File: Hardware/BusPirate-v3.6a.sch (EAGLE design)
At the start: 43 parts, among them IC1 PIC24FJ64GA002, IC2 FT232RL-BASICSSOP, IC3 4066

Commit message: Finished inital DFM
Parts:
- removed IC3: 4066, 40xx:4066
- removed ICSP: (no value), SparkFun-Connectors:M05PTH
- removed LED1A, LED2A, LED3A, LED4A: (no value), led:LEDCHIP-LED0805
- removed RN1, RN2: 10k, Testing:CAY16-F4
- removed VR3: MIC5205 5V0, SparkFun-PowerIC:MIC52055V
- added JP2: (no value), SparkFun-Connectors:M05PTH
- added LED5, LED6, LED7, LED8: RED, SparkFun-LED:LED-RED0603
- added R10, R11: 2.0k, SparkFun-Resistors:2.0KOHM1/10W5%(0603)
- added R7, R9: 1K, SparkFun-Resistors:1KOHM-1/10W-1%(0603)
- added R8: 0.27, SparkFun-Resistors:0OHM-1/10W-5%(0603)
- added U3: PIC24FJ64GA002, Testing:PIC24FJ64GA002
- added U4: MIC5205 5V0, SparkFun-PowerIC:MIC52055V
- C10, C11: value 10uF -> 0.1uF; device rcl:CPOL-EUSMCA -> SparkFun-Capacitors:0.1UF-25V(+80/-20%)(0603)
- C3, C4, C7: value 0.1uF -> 10uF; device SparkFun-Capacitors:0.1UF-25V(+80/-20%)(0603) -> SparkFun-Capacitors:10UF10V10%(0805)
- C5: device dp_devices:CAPC603 -> SparkFun-Capacitors:0.1UF-25V(+80/-20%)(0603)
- C8, C9: value 1uF -> 10uF; device dp_devices:CAPC603 -> SparkFun-Capacitors:10UF10V10%(0805)
- IC1: value PIC24FJ64GA002 -> 4066; device dp_devices:PIC24FJ64GA002 -> 40xx:4066; PROD_ID (none) -> IC-09427
- JP1: PROD_ID (none) -> CONN-09508
- L1: value 700mA+ ferrite -> 1A Ferrite; device wuerth-elektronik:WE-KIL_0805 -> SparkFun-Passives:INDUCTOR0603; PROD_ID (none) -> NDUC-12579
- LED1: value (none) -> RED; device led:LEDCHIP-LED0805 -> SparkFun-LED:LED-RED0603; PROD_ID (none) -> DIO-00819
- LED2, LED3, LED4: value (none) -> RED; device led:LEDCHIP-LED0805 -> SparkFun-LED:LED-RED0603
- LOGO1: value SFE_LOGO_NAME_FLAME.1_INCH -> OSHW-LOGOL; device SparkFun-Aesthetics:SFE_LOGO_NAME_FLAME.1_INCH -> SparkFun-Aesthetics:OSHW-LOGOL
- LOGO2: value OSHW-LOGOL -> SFE_LOGO_NAME_FLAME.1_INCH; device SparkFun-Aesthetics:OSHW-LOGOL -> SparkFun-Aesthetics:SFE_LOGO_NAME_FLAME.1_INCH
- R1, R5: value 2.0k -> 0.27; device SparkFun-Resistors:2.0KOHM1/10W5%(0603) -> SparkFun-Resistors:0OHM-1/10W-5%(0603); PROD_ID (none) -> RES-08787
- R2, R3: value 1K -> 10k; device SparkFun-Resistors:1KOHM-1/10W-1%(0603) -> Testing:CAY16-F4; PROD_ID (none) -> RES-13167
- U5: PROD_ID (none) -> IC-00870
- renumbered IC2 to U5, RN3 to R12, U$2 to J1, VR1 to U1, VR2 to U2
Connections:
- new net N$10: C7.2, R5.2
- new net N$11: C8.2, R8.2
- new net N$8: C3.2, R1.2
- net !MCLR: now also JP2.5, R10.1, U3.MCLR; no longer IC1.MCLR, ICSP.5, R1.1
- net 5V: now also C5.1, C6.1, IC1P.VDD, U4.IN; no longer C10.+, C3.1, IC3P.VDD, VR3.IN
- net ADC: now also R3C.2; no longer RN2C.2
- net ADC1: now also R3C.1, R3D.1, U3.PMD0/CN14/RP12/AN12/RB12; no longer IC1.PMD0/CN14/RP12/AN12/RB12, RN2C.1, RN2D.1
- net ADC2: now also R3A.1, R3B.1, U3.PMRD/CN13/RP13/AN11/RB13; no longer IC1.PMRD/CN13/RP13/AN11/RB13, RN2A.1, RN2B.1
- net ADC3: now also R2C.1, R2D.1, U3.PMWR/RTCC/CVREF/CN12/RP14/AN10/RB14; no longer IC1.PMWR/RTCC/CVREF/CN12/RP14/AN10/RB14, RN1C.1, RN1D.1
- net ADC4: now also R2A.1, R2B.1, U3.PMCS1/CN11/RP15/AN9/RB15; no longer IC1.PMCS1/CN11/RP15/AN9/RB15, RN1A.1, RN1B.1
- net AUX1: now also U3.PMD2/TDI/EMUD2/PGD2/CN16/RP10/RB10; no longer IC1.PMD2/TDI/EMUD2/PGD2/CN16/RP10/RB10
- net CLK: now also U3.PMD4/SCL1/TCK/CN22/RP8/RB8; no longer IC1.PMD4/SCL1/TCK/CN22/RP8/RB8
- net CS: now also U3.PMD6/ASCL1/EMUC3/PGC3/CN24/RP6/RB6; no longer IC1.PMD6/ASCL1/EMUC3/PGC3/CN24/RP6/RB6
- net CTS: now also U3.RA3/CN29/OSCO/CLKO/PMA0; no longer IC1.RA3/CN29/OSCO/CLKO/PMA0
- net GND: now also C10.2, C11.2, IC1P.VSS, JP2.3, LED4.C, LED5.C, LED6.C, LED7.C, LED8.C, R1.1, R2B.2, R2D.2, R3B.2, R3D.2, R5.1, R8.1, U3.DISVREG, U3.RB2/AN4/RP2/CN6/C1IN-/SDA2, U3.RB3/AN5/RP3/CN7/C1IN+/SCL2, U3.VSS@1, U3.VSS@2, U4.GND; no longer C10.-, C11.-, C3.2, C7.2, C8.2, IC1.DISVREG, IC1.RB2/AN4/RP2/CN6/C1IN-/SDA2, IC1.RB3/AN5/RP3/CN7/C1IN+/SCL2, IC1.VSS@1, IC1.VSS@2, IC3P.VSS, ICSP.3, LED1.C, LED1A.C, LED2.C, LED2A.C, LED3A.C, RN1B.2, RN1D.2, RN2B.2, RN2D.2, VR3.GND
- net LD1: now also R7.2, U3.RA1/AN1/CN3/VREF-; no longer IC1.RA1/AN1/CN3/VREF-, R4.2
- net MISO: now also U3.PMD5/INT0/CN23/RP7/RB7; no longer IC1.PMD5/INT0/CN23/RP7/RB7
- net MOSI: now also R11.1, U3.PMD3/SDA1/TDO/CN21/RP9/RB9; no longer IC1.PMD3/SDA1/TDO/CN21/RP9/RB9, R5.1
- net N$1: now also IC1A.B, R11.2; no longer IC3A.B, R5.2
- net N$13: now also LED1.A, LED2.A, R4.1; no longer LED4.A, LED4A.A, R3.1
- net N$18: now also LED7.A, LED8.A, R9.1; no longer LED3.A, LED3A.A, R6.1
- net N$2: now also IC1C.B; no longer IC3C.B
- net N$3: now also C9.1, U3.VCAP/VDDCORE; no longer C11.+, IC1.VCAP/VDDCORE
- net N$4: now also IC1D.B; no longer IC3D.B
- net N$5: now also IC1B.B; no longer IC3B.B
- net N$6: now also LED5.A, LED6.A, R7.1; no longer LED2.A, LED2A.A, R4.1
- net N$7: now also LED3.A, LED4.A, R6.1; no longer LED1.A, LED1A.A, R2.1
- net N$9: now also C11.1; no longer C5.1
- net PGC: now also JP2.1, U3.RB1/AN3/RP1/CN5/C2IN+/PGC1/EMUC1; no longer IC1.RB1/AN3/RP1/CN5/C2IN+/PGC1/EMUC1, ICSP.1
- net PGD: now also JP2.2, U3.RB0/AN2/RP0/CN4/C2IN-/PGD1/EMUD1; no longer IC1.RB0/AN2/RP0/CN4/C2IN-/PGD1/EMUD1, ICSP.2
- net PULLUPEN: now also IC1A.C, IC1B.C, IC1C.C, IC1D.C, U3.PMD1/TMS/EMUC2/PGC2/CN15/RP11/RB11; no longer IC1.PMD1/TMS/EMUC2/PGC2/CN15/RP11/RB11, IC3A.C, IC3B.C, IC3C.C, IC3D.C
- net RTS: now also U3.RA4/CN0/SOSCO/T1CK/PMA1; no longer IC1.RA4/CN0/SOSCO/T1CK/PMA1
- net RX: now also U3.RB4/RP4/CN1/SOSCI/PMBE; no longer IC1.RB4/RP4/CN1/SOSCI/PMBE
- net RXLED: now also LED1.C, LED2.C; no longer LED4.C, LED4A.C
- net SW3V3: now also C7.1, R2C.2, R9.2; no longer C8.1, R6.2, RN1C.2
- net SW5V0: now also C8.1, R2A.2, U4.OUT; no longer C9.1, RN1A.2, VR3.OUT
- net TP0: now also U3.RA2/CN30/OSCI/CLKI; no longer IC1.RA2/CN30/OSCI/CLKI
- net TX: now also U3.RB5/RP5/CN27/PGD3/EMUD3/ASDA1/PMD7; no longer IC1.RB5/RP5/CN27/PGD3/EMUD3/ASDA1/PMD7
- net VCC: now also C10.1, C3.1, JP2.4, R10.2, R4.2, R6.2, U3.VDD@1, U3.VDD@2; no longer C6.1, C7.1, IC1.VDD@1, IC1.VDD@2, ICSP.4, R1.2, R2.2, R3.2
- net VEXTERN: now also IC1A.A, IC1B.A, IC1C.A, IC1D.A, R3A.2; no longer IC3A.A, IC3B.A, IC3C.A, IC3D.A, RN2A.2
- net VREGEN: now also U3.RA0/AN0/CN2/VREF+, U4.EN; no longer IC1.RA0/AN0/CN2/VREF+, VR3.EN
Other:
- note added: "CABLE CONNECTOR"
- note added: "The MIC5205 requires some ESR, added 0.27Ω"
- moved on the sheet: C1, C2, C3, C4, C5, C6, C7, C8, C9, JP1, R1, R4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

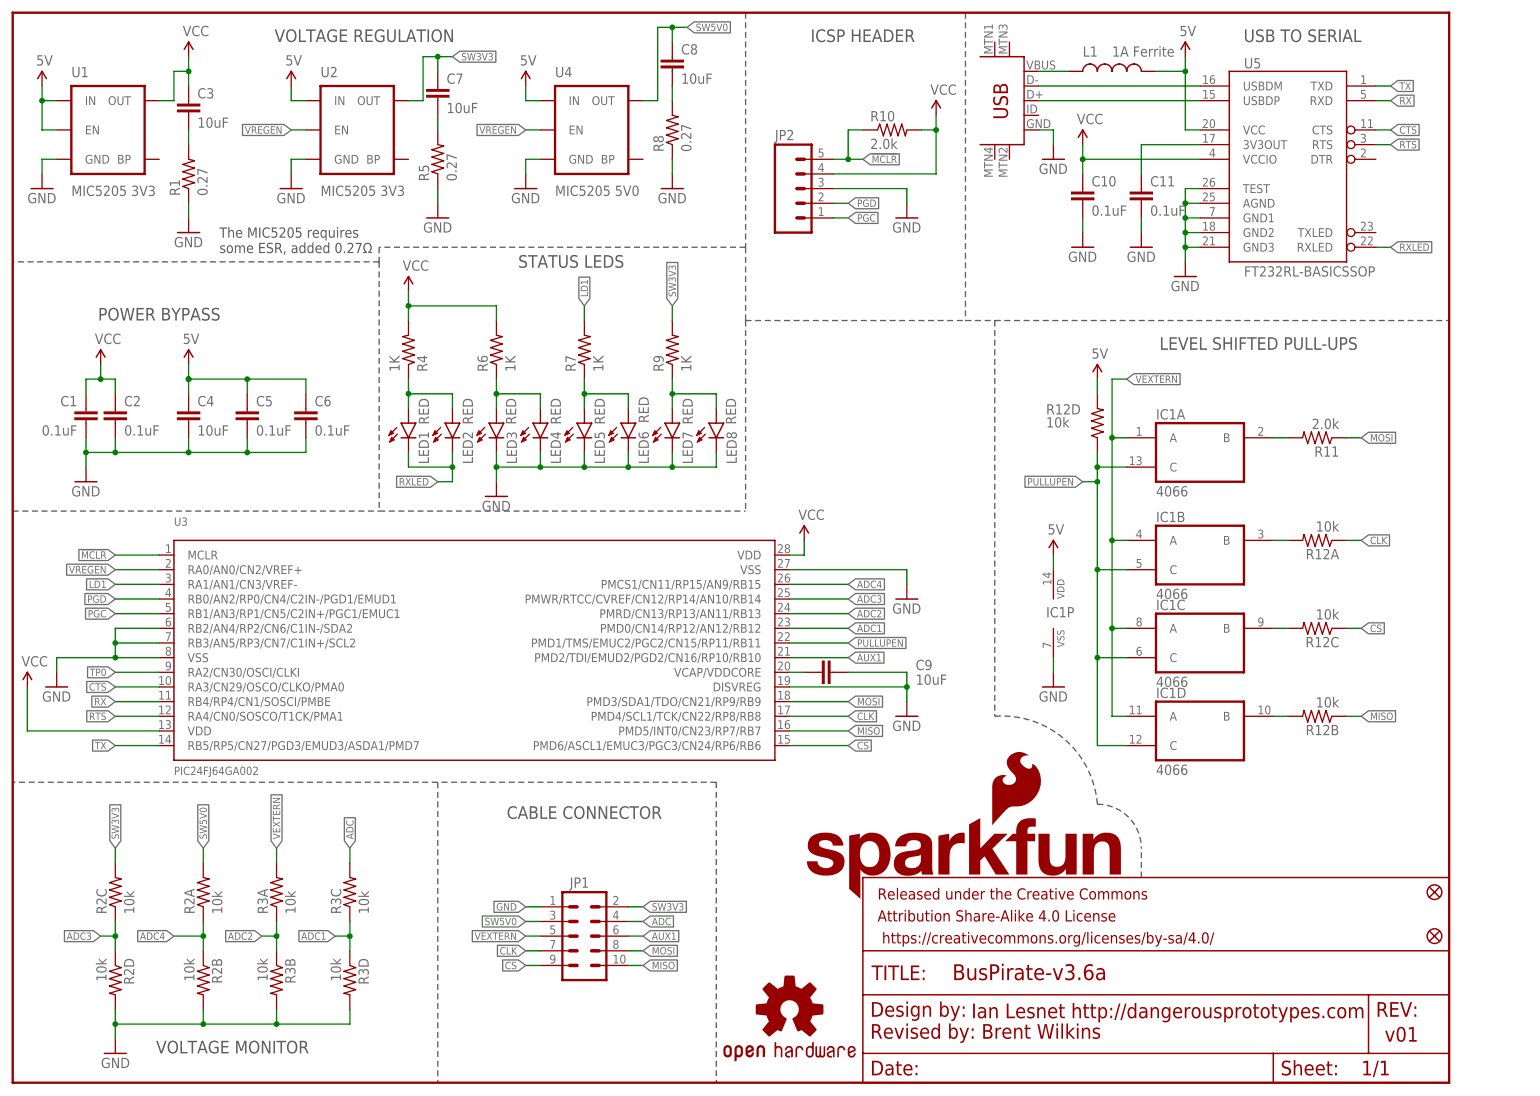
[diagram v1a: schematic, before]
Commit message: Changed from SFE to DP versioning, and changed bottom LEDs to DNP
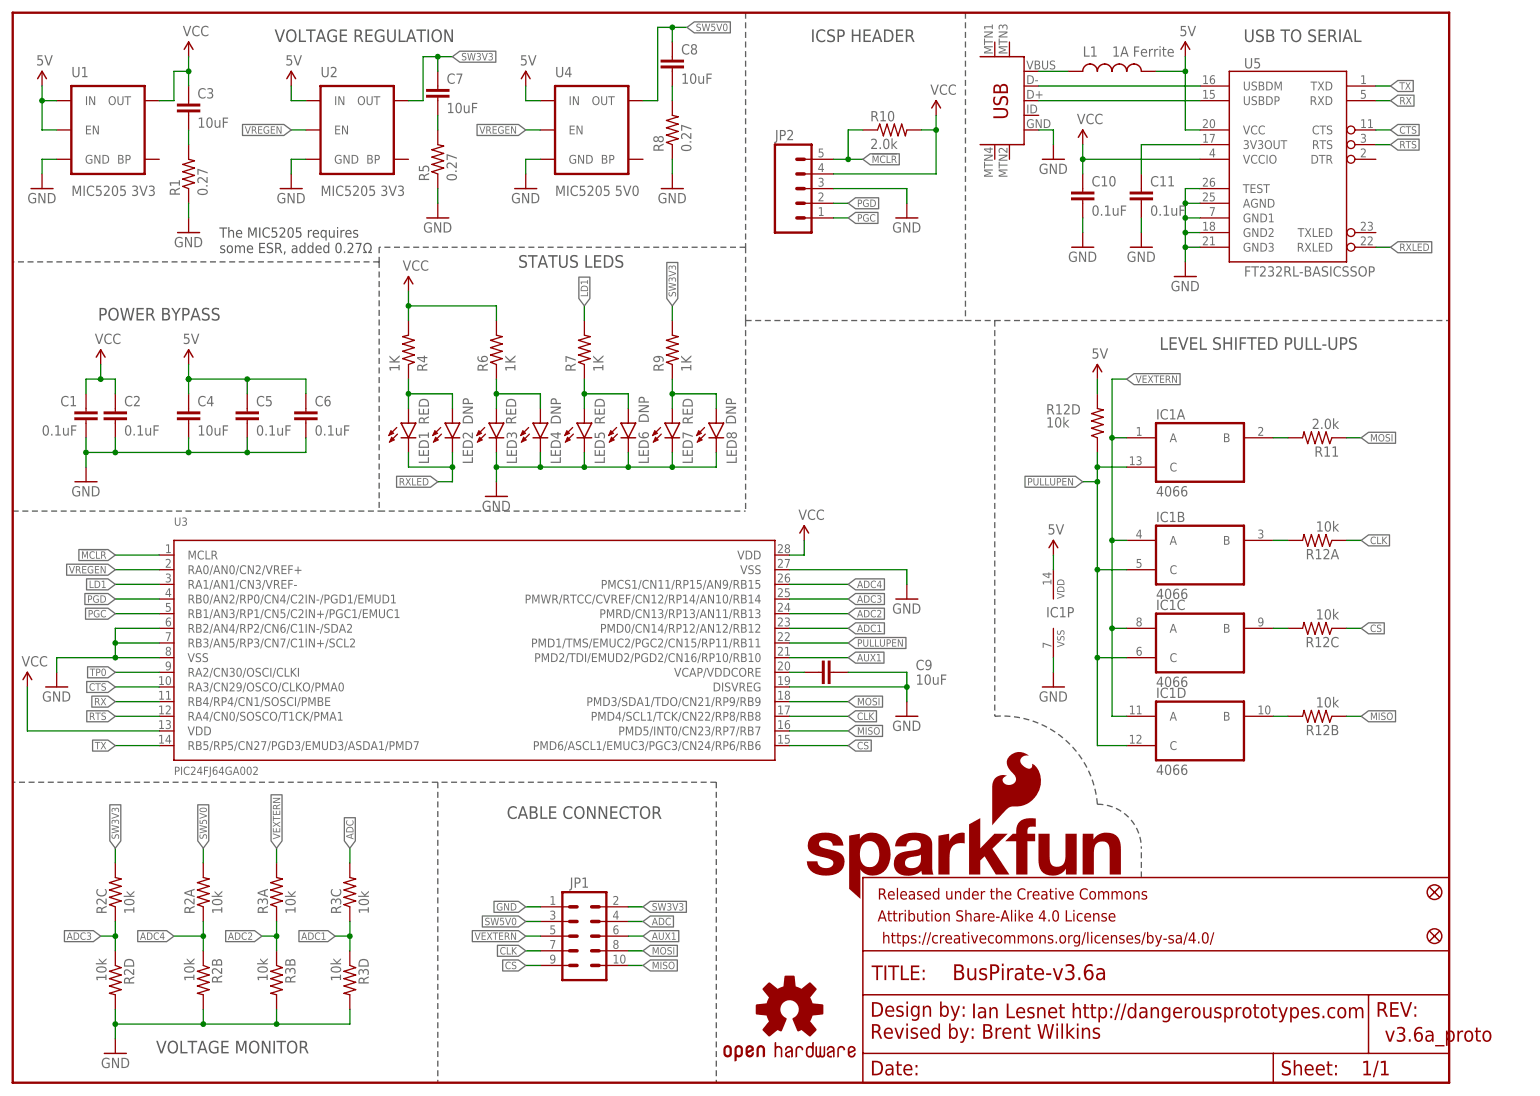
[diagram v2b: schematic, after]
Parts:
- LED2, LED4, LED6, LED8: value RED -> DNP
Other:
- note added: "v3.6a_proto"
- note removed: "v01"
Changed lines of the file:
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@@
 <part name="GND15" library="SparkFun-Aesthetics" deviceset="GND" device=""/>
 <part name="C6" library="SparkFun-Capacitors" deviceset="0.1UF-25V(+80/-20%)(0603)" device="" value="0.1uF"/>
-<part name="LED8" library="SparkFun-LED" deviceset="LED-RED" device="0603" value="RED"/>
-<part name="LED6" library="SparkFun-LED" deviceset="LED-RED" device="0603" value="RED"/>
-<part name="LED4" library="SparkFun-LED" deviceset="LED-RED" device="0603" value="RED"/>
+<part name="LED8" library="SparkFun-LED" deviceset="LED-RED" device="0603" value="DNP"/>
+<part name="LED6" library="SparkFun-LED" deviceset="LED-RED" device="0603" value="DNP"/>
+<part name="LED4" library="SparkFun-LED" deviceset="LED-RED" device="0603" value="DNP"/>
 <part name="R4" library="SparkFun-Resistors" deviceset="1KOHM-1/10W-1%(0603)" device="" value="1K"/>
 <part name="GND17" library="SparkFun-Aesthetics" deviceset="GND" device=""/>
@@
 <attribute name="PROD_ID" value="DIO-00819"/>
 </part>
-<part name="LED2" library="SparkFun-LED" deviceset="LED-RED" device="0603" value="RED"/>
+<part name="LED2" library="SparkFun-LED" deviceset="LED-RED" device="0603" value="DNP"/>
 <part name="R12" library="Testing" deviceset="CAY16-F4" device="" value="10k">
 <attribute name="PROD_ID" value="RES-13167"/>
@@
 <text x="148.59" y="7.62" size="2.54" layer="94">Revised by: Brent Wilkins</text>
 <text x="166.116" y="11.176" size="2.54" layer="94">Ian Lesnet http://dangerousprototypes.com</text>
-<text x="237.744" y="7.112" size="2.54" layer="94">v01</text>
+<text x="237.744" y="7.112" size="2.54" layer="94">v3.6a_proto</text>
 <text x="60.96" y="180.34" size="2.1844" layer="97" font="vector" ratio="15" align="bottom-center">VOLTAGE REGULATION</text>
 <wire x1="121.92" y1="52.07" x2="73.66" y2="52.07" width="0.1524" layer="97" style="shortdash"/>
